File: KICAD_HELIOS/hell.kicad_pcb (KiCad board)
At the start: 4 copper layers, 109 x 86 mm, 171 parts, among them J101 NC3FAAH, J102 NC3MAAH, J103 ecran, J104 Conn_ST_STDC14, J105 Conn_01x02, SW101 SW_Push, SW102 SW_Push, SW103 SW_Push, U101 R-78B5.0-2.0, U102 AZ1117CH2-3.3TRG1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

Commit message: pcb
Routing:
- net GND: track 160.0 -> 177.6 mm, vias 57 -> 69
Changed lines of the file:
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@@
 	)
 	(segment
+		(start 125.4875 79.3)
+		(end 126.9 79.3)
+		(width 0.2)
+		(layer "F.Cu")
+		(net 1)
+	)
+	(segment
 		(start 94.445 98.675)
 		(end 90.5 98.675)
@@
 	)
 	(segment
+		(start 124.97 66.095)
+		(end 124.97 65.43)
+		(width 0.2)
+		(layer "F.Cu")
+		(net 1)
+	)
+	(segment
 		(start 185.2 77.5)
 		(end 187.1 77.5)
@@
 	)
 	(segment
+		(start 119.825 61.875)
+		(end 119.8 61.9)
+		(width 0.2)
+		(layer "F.Cu")
+		(net 1)
+	)
+	(segment
 		(start 119.38 117.1)
 		(end 120.6 117.1)
@@
 	)
 	(segment
+		(start 124.97 65.43)
+		(end 125.4 65)
+		(width 0.2)
+		(layer "F.Cu")
+		(net 1)
+	)
+	(segment
 		(start 185.2 100)
 		(end 187.1 100)
@@
 	)
 	(segment
+		(start 119.825 71.8)
+		(end 118.6 71.8)
+		(width 0.2)
+		(layer "F.Cu")
+		(net 1)
+	)
+	(segment
 		(start 185.2 104.5)
 		(end 187.1 104.5)
@@
 	)
 	(segment
+		(start 124.97 54.33)
+		(end 125.4 53.9)
+		(width 0.2)
+		(layer "F.Cu")
+		(net 1)
+	)
+	(segment
+		(start 114.55 64.2)
+		(end 116 64.2)
+		(width 1)
+		(layer "F.Cu")
+		(net 1)
+	)
+	(segment
 		(start 185.2 107.5)
 		(end 187.1 107.5)
@@
 	)
 	(segment
-		(start 117.18 93.18)
-		(end 117.2 93.2)
+		(start 119.825 60.8)
+		(end 119.825 61.875)
 		(width 0.2)
 		(layer "F.Cu")
@@
 	)
 	(segment
+		(start 124.97 83.395)
+		(end 124.97 82.23)
+		(width 0.2)
+		(layer "F.Cu")
+		(net 1)
+	)
+	(segment
 		(start 112.13 66.535)
 		(end 112.215 66.535)
@@
 	)
 	(segment
+		(start 119.825 90.875)
+		(end 119 91.7)
+		(width 0.2)
+		(layer "F.Cu")
+		(net 1)
+	)
+	(segment
+		(start 111.69 120.99)
+		(end 111.7 121)
+		(width 0.2)
+		(layer "F.Cu")
+		(net 1)
+	)
+	(segment
 		(start 185.2 53.5)
 		(end 187.1 53.5)
@@
 	)
 	(segment
+		(start 125.475 77.4)
+		(end 126.9 77.4)
+		(width 0.2)
+		(layer "F.Cu")
+		(net 1)
+	)
+	(segment
 		(start 107.85 64.2)
 		(end 114.55 64.2)
@@
 	)
 	(segment
+		(start 112.96 119.3)
+		(end 112.96 120.96)
+		(width 0.2)
+		(layer "F.Cu")
+		(net 1)
+	)
+	(segment
 		(start 112.75 82.5125)
 		(end 112.75 84.147919)
@@
 	)
 	(segment
+		(start 124.97 55.095)
+		(end 124.97 54.33)
+		(width 0.2)
+		(layer "F.Cu")
+		(net 1)
+	)
+	(segment
 		(start 185.2 71.5)
 		(end 187.1 71.5)
@@
 	)
 	(segment
+		(start 111.69 119.3)
+		(end 111.69 120.99)
+		(width 0.2)
+		(layer "F.Cu")
+		(net 1)
+	)
+	(segment
 		(start 185.2 86.5)
 		(end 187.1 86.5)
@@
 	)
 	(segment
+		(start 112.96 120.96)
+		(end 113 121)
+		(width 0.2)
+		(layer "F.Cu")
+		(net 1)
+	)
+	(segment
 		(start 185.2 110.5)
 		(end 187.1 110.5)
@@
 	)
 	(segment
+		(start 119.825 60.875)
+		(end 119.8 60.9)
+		(width 0.2)
+		(layer "F.Cu")
+		(net 1)
+	)
+	(segment
 		(start 124.97 94.395)
 		(end 126.695 94.395)
@@
 	)
 	(segment
+		(start 124.97 82.23)
+		(end 125.5 81.7)
+		(width 0.2)
+		(layer "F.Cu")
+		(net 1)
+	)
+	(segment
 		(start 126.695 94.395)
 		(end 126.7 94.4)
@@
 	)
 	(segment
+		(start 119.825 60.8)
+		(end 119.825 60.875)
+		(width 0.2)
+		(layer "F.Cu")
+		(net 1)
+	)
+	(segment
 		(start 103.175 46.3)
 		(end 104.825 46.3)
@@
 	)
 	(segment
+		(start 119.825 89.1)
+		(end 119.825 90.875)
+		(width 0.2)
+		(layer "F.Cu")
+		(net 1)
+	)
+	(segment
 		(start 185.2 68.5)
 		(end 187.1 68.5)
@@
 	)
 	(via
+		(at 119.8 61.9)
+		(size 0.6)
+		(drill 0.3)
+		(layers "F.Cu" "B.Cu")
+		(net 1)
+	)
+	(via
 		(at 187.1 65.5)
 		(size 1)
@@
 	)
 	(via
+		(at 126.9 77.4)
+		(size 0.6)
+		(drill 0.3)
+		(layers "F.Cu" "B.Cu")
+		(net 1)
+	)
+	(via
 		(at 107.4 70.4)
 		(size 1)
@@
 	)
 	(via
+		(at 126.9 79.3)
+		(size 0.6)
+		(drill 0.3)
+		(layers "F.Cu" "B.Cu")
+		(net 1)
+	)
+	(via
 		(at 187.1 41.5)
 		(size 1)
@@
 	)
 	(via
+		(at 113 121)
+		(size 0.6)
+		(drill 0.3)
+		(layers "F.Cu" "B.Cu")
+		(net 1)
+	)
+	(via
 		(at 187.1 116.5)
 		(size 1)
@@
 	)
 	(via
+		(at 125.5 81.7)
+		(size 0.6)
+		(drill 0.3)
+		(layers "F.Cu" "B.Cu")
+		(net 1)
+	)
+	(via
 		(at 120.6 117.1)
 		(size 0.6)
@@
 	)
 	(via
+		(at 111.7 121)
+		(size 0.6)
+		(drill 0.3)
+		(layers "F.Cu" "B.Cu")
+		(net 1)
+	)
+	(via
 		(at 187.1 74.5)
 		(size 1)
@@
 	)
 	(via
+		(at 118.6 71.8)
+		(size 0.6)
+		(drill 0.3)
+		(layers "F.Cu" "B.Cu")
+		(net 1)
+	)
+	(via
 		(at 187.1 44.5)
 		(size 1)
@@
 	)
 	(via
+		(at 119 91.7)
+		(size 0.6)
+		(drill 0.3)
+		(layers "F.Cu" "B.Cu")
+		(net 1)
+	)
+	(via
 		(at 187.1 40)
 		(size 1)
@@
 	)
 	(via
+		(at 116 64.2)
+		(size 0.6)
+		(drill 0.3)
+		(layers "F.Cu" "B.Cu")
+		(net 1)
+	)
+	(via
 		(at 187.1 98.5)
 		(size 1)
@@
 	)
 	(via
+		(at 125.4 65)
+		(size 0.6)
+		(drill 0.3)
+		(layers "F.Cu" "B.Cu")
+		(net 1)
+	)
+	(via
 		(at 187.1 104.5)
 		(size 1)
@@
 	)
 	(via
+		(at 126.9 77.4)
+		(size 0.6)
+		(drill 0.3)
+		(layers "F.Cu" "B.Cu")
+		(net 1)
+	)
+	(via
 		(at 111.6 55.5)
 		(size 0.6)
@@
 	)
 	(via
+		(at 125.4 53.9)
+		(size 0.6)
+		(drill 0.3)
+		(layers "F.Cu" "B.Cu")
+		(net 1)
+	)
+	(via
 		(at 114.9 112.8)
 		(size 0.6)
@@
 		(net 1)
 		(net_name "GND")
+		(locked yes)
 		(layers "F.Cu" "B.Cu")
 		(hatch edge 0.5)

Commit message: pcb
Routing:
- net GND: track 177.6 -> 192.2 mm, vias 69 -> 72

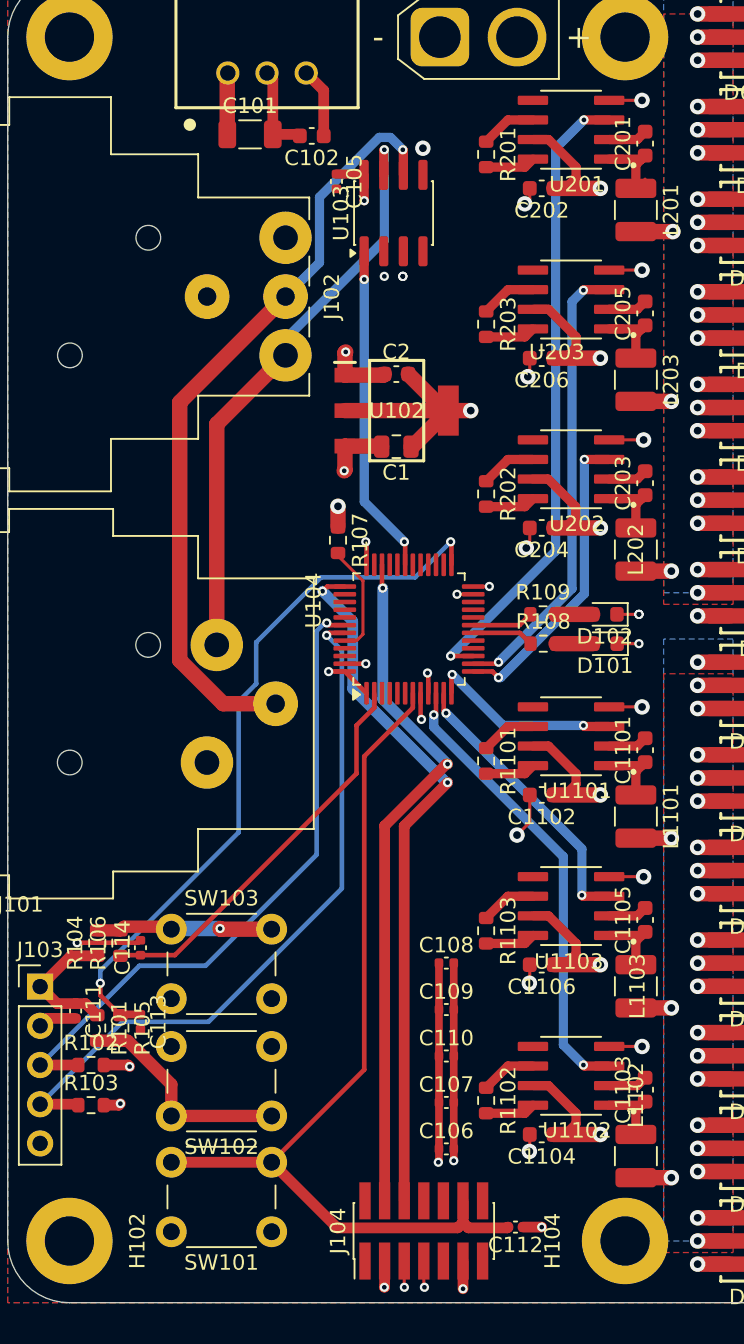
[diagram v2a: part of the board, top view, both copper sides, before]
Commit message: pcb pour impression
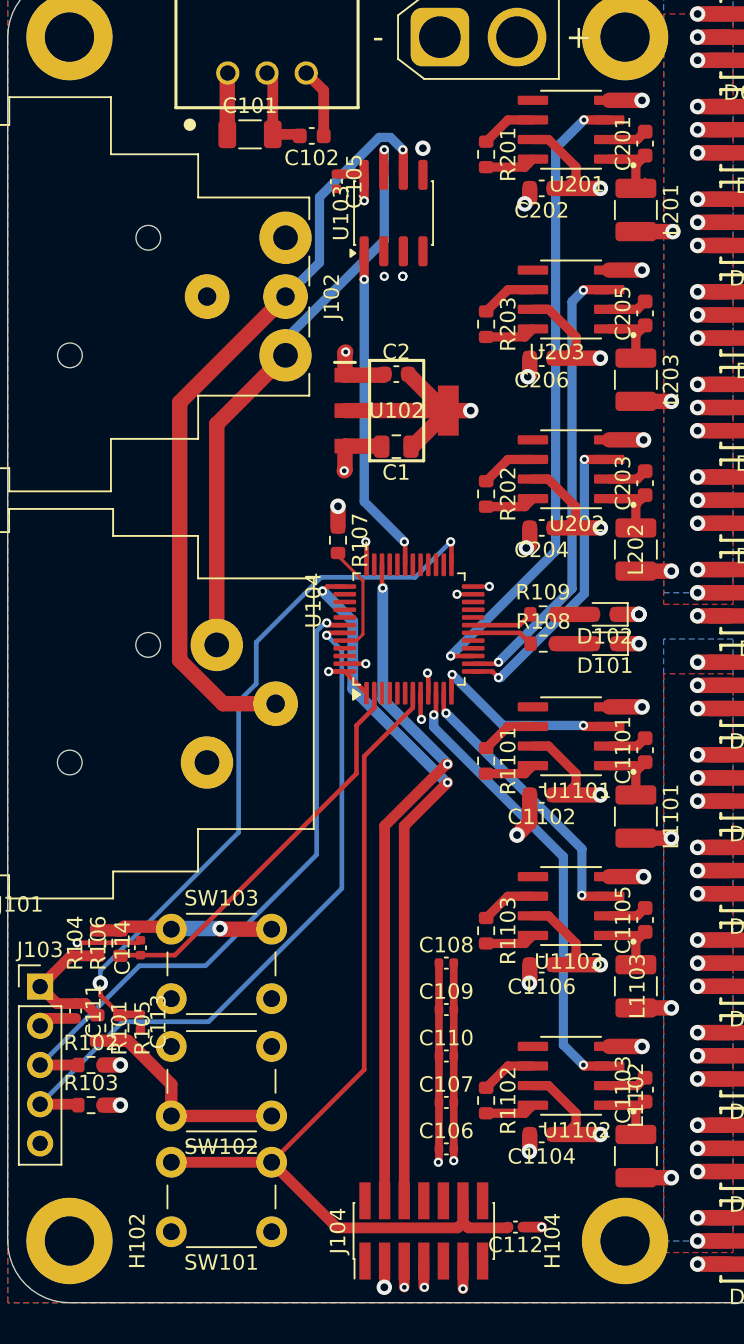
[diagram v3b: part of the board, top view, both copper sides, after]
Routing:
- net +3.3V: track 37.4 -> 36.7 mm
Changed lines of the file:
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@@
 	)
 	(paper "A4")
+	(title_block
+		(title "PCB HELIOS 1AB 2026")
+	)
 	(layers
 		(0 "F.Cu" signal)
@@
 		(start 125.4875 79.3)
 		(end 126.9 79.3)
-		(width 0.2)
+		(width 1)
 		(layer "F.Cu")
 		(net 1)
@@
 		(start 124.97 44.095)
 		(end 127.095 44.095)
-		(width 0.2)
+		(width 1)
 		(layer "F.Cu")
 		(net 1)
@@
 		(start 119.825 100.1)
 		(end 119.825 101.275)
-		(width 0.2)
+		(width 1)
 		(layer "F.Cu")
 		(net 1)
@@
 		(start 119.825 49.8)
 		(end 119.825 50.475)
-		(width 0.2)
+		(width 1)
 		(layer "F.Cu")
 		(net 1)
@@
 		(start 119.825 90.875)
 		(end 119 91.7)
-		(width 0.2)
+		(width 1)
 		(layer "F.Cu")
 		(net 1)
@@
 		(start 125.475 77.4)
 		(end 126.9 77.4)
-		(width 0.2)
+		(width 1)
 		(layer "F.Cu")
 		(net 1)
@@
 		(start 112.96 119.3)
 		(end 112.96 120.96)
-		(width 0.2)
+		(width 0.7)
 		(layer "F.Cu")
 		(net 1)
@@
 		(start 111.69 119.3)
 		(end 111.69 120.99)
-		(width 0.2)
+		(width 0.7)
 		(layer "F.Cu")
 		(net 1)
@@
 		(start 119.825 71.8)
 		(end 119.825 72.875)
-		(width 0.2)
+		(width 1)
 		(layer "F.Cu")
 		(net 1)
@@
 		(start 124.97 83.395)
 		(end 127.095 83.395)
-		(width 0.2)
+		(width 1)
 		(layer "F.Cu")
 		(net 1)
@@
 		(start 119.825 111.1)
 		(end 119.825 112.175)
-		(width 0.2)
+		(width 1)
 		(layer "F.Cu")
 		(net 1)
@@
 		(start 124.97 105.395)
 		(end 127.095 105.395)
-		(width 0.2)
+		(width 1)
 		(layer "F.Cu")
 		(net 1)
@@
 		(start 124.97 55.095)
 		(end 127.095 55.095)
-		(width 0.2)
+		(width 1)
 		(layer "F.Cu")
 		(net 1)
@@
 		(start 119.825 60.8)
 		(end 119.825 61.875)
-		(width 0.2)
+		(width 1)
 		(layer "F.Cu")
 		(net 1)
@@
 		(start 119.825 89.1)
 		(end 119.825 90.875)
-		(width 0.2)
+		(width 1)
 		(layer "F.Cu")
 		(net 1)
@@
 		(start 124.97 66.095)
 		(end 127.195 66.095)
-		(width 0.2)
+		(width 1)
 		(layer "F.Cu")
 		(net 1)
@@
 		(start 124.97 94.395)
 		(end 127.195 94.395)
-		(width 0.2)
+		(width 1)
 		(layer "F.Cu")
 		(net 1)
@@
 	(via
 		(at 126.9 77.4)
-		(size 0.6)
-		(drill 0.3)
+		(size 1)
+		(drill 0.5)
 		(layers "F.Cu" "B.Cu")
 		(net 1)
@@
 	(via
 		(at 126.9 79.3)
-		(size 0.6)
-		(drill 0.3)
+		(size 1)
+		(drill 0.5)
 		(layers "F.Cu" "B.Cu")
 		(net 1)
@@
 	(via
 		(at 126.9 77.4)
-		(size 0.6)
-		(drill 0.3)
+		(size 1)
+		(drill 0.5)
 		(layers "F.Cu" "B.Cu")
 		(net 1)
@@
 	)
 	(segment
-		(start 92.225 109.2)
-		(end 93.2 109.2)
-		(width 0.7)
-		(layer "F.Cu")
-		(net 2)
-	)
-	(segment
 		(start 113.94 112.035)
 		(end 113.94 112.86)
@@
 	)
 	(segment
+		(start 92.225 109.2)
+		(end 93.3 109.2)
+		(width 1)
+		(layer "F.Cu")
+		(net 2)
+	)
+	(segment
 		(start 109.25 82.5125)
 		(end 107.8375 81.1)
@@
 	)
 	(segment
-		(start 93.2 109.2)
-		(end 93.3 109.1)
-		(width 0.7)
-		(layer "F.Cu")
-		(net 2)
-	)
-	(segment
 		(start 107.8375 81.1)
 		(end 106.80055 81.1)
@@
 	)
 	(segment
-		(start 93.8 106.6)
-		(end 93.9 106.7)
-		(width 0.7)
-		(layer "F.Cu")
-		(net 2)
-	)
-	(segment
-		(start 92.225 106.6)
-		(end 93.8 106.6)
-		(width 0.7)
-		(layer "F.Cu")
-		(net 2)
-	)
-	(segment
 		(start 107.85 68.05)
 		(end 107.8 68.1)
@@
 	)
 	(segment
+		(start 92.225 106.6)
+		(end 93.3 106.6)
+		(width 1)
+		(layer "F.Cu")
+		(net 2)
+	)
+	(segment
 		(start 113.94 103.005)
 		(end 113.94 106.015)
@@
 	)
 	(via
-		(at 93.9 106.7)
-		(size 0.6)
-		(drill 0.3)
+		(at 93.3 106.6)
+		(size 1)
+		(drill 0.5)
 		(layers "F.Cu" "B.Cu")
 		(net 2)
@@
 	(via
 		(at 110.4 121)
-		(size 0.6)
-		(drill 0.3)
+		(size 1)
+		(drill 0.5)
 		(layers "F.Cu" "B.Cu")
 		(net 2)
 	)
 	(via
-		(at 93.3 109.1)
-		(size 0.6)
-		(drill 0.3)
+		(at 93.3 109.2)
+		(size 1)
+		(drill 0.5)
 		(layers "F.Cu" "B.Cu")
 		(net 2)
@@
 	(via
 		(at 99.757049 97.757049)
-		(size 0.6)
-		(drill 0.3)
+		(size 1)
+		(drill 0.5)
 		(layers "F.Cu" "B.Cu")
 		(net 294)
@@
 	(via
 		(at 92 101.3)
-		(size 0.6)
-		(drill 0.3)
+		(size 1)
+		(drill 0.5)
 		(layers "F.Cu" "B.Cu")
 		(net 300)
